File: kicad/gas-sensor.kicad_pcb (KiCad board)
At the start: 2 copper layers, 37 parts, among them J1 Conn FT232RL, J10 hole, J11 hole, J2 RJ12, J3 hole, J4 hole, J5 hole, J6 hole, J7 5V_Power_source, J8 hole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

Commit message: Update after debugging
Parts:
- moved J10 9.09 mm to (59.9, 66.5)
- moved J8 9.09 mm to (140.2, 66.5)
- moved J11 9.09 mm to (59.9, 94.2)
- moved J9 9.09 mm to (140.2, 94.2)
- moved U3 2.13 mm to (72.6, 94.2)
- moved GS1 1.48 mm to (130.8, 84.9)
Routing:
- net Net-(GS1-Pad6): track 31.7 -> 29.8 mm
- net /HUM: track 85.7 -> 86.7 mm
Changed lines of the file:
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@@
-(kicad_pcb (version 20171130) (host pcbnew "(5.0.2-4-g3082e92af)")
+(kicad_pcb (version 20171130) (host pcbnew "(5.0.1-3-g963ef8bb5)")
   (general
     (thickness 1.6)
     (drawings 12)
-    (tracks 384)
+    (tracks 383)
     (zones 0)
     (modules 37)
@@
   )
   (setup
-    (last_trace_width 0.25)
+    (last_trace_width 1)
     (user_trace_width 0.25)
     (user_trace_width 0.5)
@@
     (add_net VCC)
   )
+  (module footprints:DHT22_HOR (layer F.Cu)
+    (at 72.61 94.22)
+    (fp_text reference U3 (at -0.72 1.86) (layer F.SilkS)
+      (effects (font (size 1 1) (thickness 0.15)))
+    )
+    (fp_text value DHT22 (at -0.79 -1.8) (layer F.Fab)
+      (effects (font (size 1 1) (thickness 0.15)))
+    )
+    (fp_line (start 6.3 -30) (end 6.3 3) (layer F.SilkS) (width 0.15))
+    (fp_line (start -8.8 -30) (end -8.8 3) (layer F.SilkS) (width 0.15))
+    (fp_line (start -8.8 -30) (end 6.3 -30) (layer F.SilkS) (width 0.15))
+    (fp_line (start 6.3 3) (end -8.8 3) (layer F.SilkS) (width 0.15))
+    (pad 4 thru_hole rect (at 2.54 0) (size 1.5 1.5) (drill oval 1 0.8) (layers *.Cu *.Mask)
+      (net 1 GND))
+    (pad 3 thru_hole rect (at 0 0) (size 1.5 1.5) (drill oval 1 0.8) (layers *.Cu *.Mask)
+      (net 46 "Net-(U3-Pad3)"))
+    (pad 2 thru_hole rect (at -2.54 0) (size 1.5 1.5) (drill oval 1 0.8) (layers *.Cu *.Mask)
+      (net 25 /HUM))
+    (pad 1 thru_hole rect (at -5 0) (size 1.5 1.5) (drill oval 1 0.8) (layers *.Cu *.Mask)
+      (net 7 +5V))
+    (model ${KIPRJMOD}/shapes3D/DHT22_HOR.wrl
+      (offset (xyz -9 5 0))
+      (scale (xyz 400 400 400))
+      (rotate (xyz 0 0 0))
+    )
+  )
   (module footprints:MH-Z19 (layer F.Cu)
     (at 90.25 80.37 270)
@@
       (at (xyz 0 0 0))
       (scale (xyz 1 1 1))
-      (rotate (xyz 0 0 0))
-    )
-  )
-  (module footprints:DHT22_HOR (layer F.Cu)
-    (at 70.48 94.34)
-    (fp_text reference U3 (at -0.72 1.86) (layer F.SilkS)
-      (effects (font (size 1 1) (thickness 0.15)))
-    )
-    (fp_text value DHT22 (at -0.79 -1.8) (layer F.Fab)
-      (effects (font (size 1 1) (thickness 0.15)))
-    )
-    (fp_line (start 6.3 3) (end -8.8 3) (layer F.SilkS) (width 0.15))
-    (fp_line (start -8.8 -30) (end 6.3 -30) (layer F.SilkS) (width 0.15))
-    (fp_line (start -8.8 -30) (end -8.8 3) (layer F.SilkS) (width 0.15))
-    (fp_line (start 6.3 -30) (end 6.3 3) (layer F.SilkS) (width 0.15))
-    (pad 4 thru_hole rect (at 2.5 0) (size 1 1) (drill 0.5) (layers *.Cu *.Mask)
-      (net 1 GND))
-    (pad 3 thru_hole rect (at 0 0) (size 1 1) (drill 0.5) (layers *.Cu *.Mask)
-      (net 46 "Net-(U3-Pad3)"))
-    (pad 2 thru_hole rect (at -2.5 0) (size 1 1) (drill 0.5) (layers *.Cu *.Mask)
-      (net 25 /HUM))
-    (pad 1 thru_hole rect (at -5 0) (size 1 1) (drill 0.5) (layers *.Cu *.Mask)
-      (net 7 +5V))
-    (model ${KIPRJMOD}/shapes3D/DHT22_HOR.wrl
-      (offset (xyz -9 5 0))
-      (scale (xyz 400 400 400))
       (rotate (xyz 0 0 0))
     )
@@
   )
   (module MountingHole:MountingHole_3.2mm_M3 (layer F.Cu)
-    (at 146.65 60.15)
+    (at 140.15 66.5)
     (descr "Mounting Hole 3.2mm, no annular, M3")
     (tags "mounting hole 3.2mm no annular m3")
@@
   )
   (module MountingHole:MountingHole_3.2mm_M3 (layer F.Cu)
-    (at 146.65 100.5)
+    (at 140.15 94.15)
     (descr "Mounting Hole 3.2mm, no annular, M3")
     (tags "mounting hole 3.2mm no annular m3")
@@
   )
   (module MountingHole:MountingHole_3.2mm_M3 (layer F.Cu)
-    (at 53.35 60.15)
+    (at 59.85 66.5)
     (descr "Mounting Hole 3.2mm, no annular, M3")
     (tags "mounting hole 3.2mm no annular m3")
@@
   )
   (module MountingHole:MountingHole_3.2mm_M3 (layer F.Cu)
-    (at 53.35 100.5)
+    (at 59.85 94.15)
     (descr "Mounting Hole 3.2mm, no annular, M3")
     (tags "mounting hole 3.2mm no annular m3")
@@
   )
   (module footprints:MQ-4 (layer F.Cu)
-    (at 132.28 85.13 180)
+    (at 130.82 84.89 180)
     (fp_text reference GS1 (at 0 1.27 180) (layer F.SilkS)
       (effects (font (size 1 1) (thickness 0.15)))
@@
   )
   (gr_line (start 56.7 63.15) (end 143.7 63.15) (layer F.SilkS) (width 0.2))
-  (gr_line (start 143.7 63.15) (end 143.7 97.5) (layer F.SilkS) (width 0.2))
+  (gr_line (start 143.5 63.15) (end 143.5 97.5) (layer F.SilkS) (width 0.2))
   (gr_line (start 56.7 97.5) (end 143.3 97.5) (layer F.SilkS) (width 0.2))
-  (gr_line (start 56.7 63.15) (end 56.7 97.5) (layer F.SilkS) (width 0.2))
+  (gr_line (start 56.5 63.15) (end 56.5 97.5) (layer F.SilkS) (width 0.2))
   (gr_line (start 150 103.5) (end 50 103.5) (layer F.SilkS) (width 0.2))
   (gr_line (start 50 57.15) (end 150 57.15) (layer F.SilkS) (width 0.2))
@@
   (segment (start 116.55499 118.41501) (end 116.55499 118.34649) (width 1) (layer F.Cu) (net 16))
   (segment (start 115.78 119.19) (end 116.55499 118.41501) (width 1) (layer F.Cu) (net 16))
-  (segment (start 134.638751 87.488751) (end 135.63875 88.48875) (width 1) (layer F.Cu) (net 16))
-  (segment (start 129.921249 87.488751) (end 134.638751 87.488751) (width 1) (layer F.Cu) (net 16))
-  (segment (start 128.92125 88.48875) (end 129.921249 87.488751) (width 1) (layer F.Cu) (net 16))
-  (segment (start 116.55499 100.85501) (end 128.92125 88.48875) (width 1) (layer F.Cu) (net 16))
   (segment (start 116.55499 118.41501) (end 116.55499 100.85501) (width 1) (layer F.Cu) (net 16))
+  (segment (start 127.46125 89.94875) (end 127.46125 88.24875) (width 1) (layer F.Cu) (net 16))
+  (segment (start 116.55499 100.85501) (end 127.46125 89.94875) (width 1) (layer F.Cu) (net 16))
+  (segment (start 133.178751 87.248751) (end 134.17875 88.24875) (width 1) (layer F.Cu) (net 16))
+  (segment (start 128.461249 87.248751) (end 133.178751 87.248751) (width 1) (layer F.Cu) (net 16))
+  (segment (start 127.46125 88.24875) (end 128.461249 87.248751) (width 1) (layer F.Cu) (net 16))
   (segment (start 93.142934 126.012755) (end 92.73 125.599821) (width 0.5) (layer F.Cu) (net 17))
   (segment (start 93.917934 126.012755) (end 93.142934 126.012755) (width 0.5) (layer F.Cu) (net 17))
@@
   (via (at 78.41 137.98) (size 0.8) (drill 0.4) (layers F.Cu B.Cu) (net 25))
   (segment (start 81.5 137.98) (end 78.41 137.98) (width 0.5) (layer B.Cu) (net 25))
-  (segment (start 78.38 138.01) (end 78.41 137.98) (width 0.5) (layer F.Cu) (net 25))
-  (segment (start 73.88 138.01) (end 78.38 138.01) (width 0.5) (layer F.Cu) (net 25))
-  (segment (start 63.57999 127.70999) (end 63.49999 127.70999) (width 0.5) (layer F.Cu) (net 25))
-  (segment (start 73.88 138.01) (end 63.57999 127.70999) (width 0.5) (layer F.Cu) (net 25))
-  (segment (start 63.49999 127.70999) (end 61.33 125.54) (width 0.5) (layer F.Cu) (net 25))
-  (segment (start 61.33 125.54) (end 53.25 125.54) (width 0.5) (layer F.Cu) (net 25))
-  (segment (start 67.98 95.34) (end 67.98 94.34) (width 0.5) (layer F.Cu) (net 25))
-  (segment (start 67.98 100.111002) (end 67.98 95.34) (width 0.5) (layer F.Cu) (net 25))
-  (segment (start 51.869999 116.221003) (end 67.98 100.111002) (width 0.5) (layer F.Cu) (net 25))
+  (segment (start 51.869999 116.221003) (end 70.07 98.021002) (width 0.5) (layer F.Cu) (net 25))
   (segment (start 51.869999 124.159999) (end 51.869999 116.221003) (width 0.5) (layer F.Cu) (net 25))
   (segment (start 53.25 125.54) (end 51.869999 124.159999) (width 0.5) (layer F.Cu) (net 25))
-  (segment (start 128.53 116.57) (end 127.03 116.57) (width 0.5) (layer F.Cu) (net 26))
-  (segment (start 131.890002 116.57) (end 128.53 116.57) (width 0.5) (layer F.Cu) (net 26))
-  (segment (start 132.28 116.180002) (end 131.890002 116.57) (width 0.5) (layer F.Cu) (net 26))
-  (segment (start 132.28 89.88) (end 132.28 116.180002) (width 0.5) (layer F.Cu) (net 26))
+  (segment (start 63.49999 127.70999) (end 61.33 125.54) (width 0.5) (layer F.Cu) (net 25))
+  (segment (start 73.88 138.01) (end 63.57999 127.70999) (width 0.5) (layer F.Cu) (net 25))
+  (segment (start 70.07 98.021002) (end 70.07 94.22) (width 0.5) (layer F.Cu) (net 25))
+  (segment (start 61.33 125.54) (end 53.25 125.54) (width 0.5) (layer F.Cu) (net 25))
+  (segment (start 63.57999 127.70999) (end 63.49999 127.70999) (width 0.5) (layer F.Cu) (net 25))
+  (segment (start 78.38 138.01) (end 73.88 138.01) (width 0.5) (layer F.Cu) (net 25))
+  (segment (start 78.41 137.98) (end 78.38 138.01) (width 0.5) (layer F.Cu) (net 25))
+  (segment (start 129.17 116.57) (end 127.03 116.57) (width 0.5) (layer F.Cu) (net 26))
+  (segment (start 130.82 114.92) (end 129.17 116.57) (width 0.5) (layer F.Cu) (net 26))
+  (segment (start 130.82 89.64) (end 130.82 114.92) (width 0.5) (layer F.Cu) (net 26))
   (segment (start 102.052936 128.262755) (end 102.94 127.375691) (width 0.5) (layer F.Cu) (net 27))
   (segment (start 100.967934 128.262755) (end 102.052936 128.262755) (width 0.5) (layer F.Cu) (net 27))

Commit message: Update
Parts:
- added R6: 4,7k, Resistor_SMD:R_0805_2012Metric_Pad1.15x1.40mm_HandSolder, F.Cu at (105.8, 104.8)
- R2: value R -> 4,7
- R4: value 20k -> 22k
- moved J7 3.11 mm to (64.8, 131.2)
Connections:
- DS1 pad 10: Net-(DS1-Pad10) -> (no net)
- DS1 pad 3: VCC -> (no net)
- DS1 pad 5: /LCD_RW -> GND
- DS1 pad 7: Net-(DS1-Pad7) -> (no net)
- DS1 pad 8: Net-(DS1-Pad8) -> (no net)
- DS1 pad 9: Net-(DS1-Pad9) -> (no net)
- GS3 pad 2: /RX_MH-Z19 -> /TX_MH-Z19
- GS3 pad 3: /TX_MH-Z19 -> /RX_MH-Z19
- GS3 pad 4: Net-(GS3-Pad4) -> (no net)
- GS3 pad 5: Net-(GS3-Pad5) -> (no net)
- GS3 pad 6: VCC -> +5V
- GS3 pad 8: Net-(GS3-Pad8) -> (no net)
- J1 pad 2: Net-(J1-Pad2) -> (no net)
- J10 pad 1: Net-(J10-Pad1) -> (no net)
- J11 pad 1: Net-(J11-Pad1) -> (no net)
- J2 pad 1: Net-(J2-Pad1) -> (no net)
- J2 pad 5: Net-(J2-Pad5) -> (no net)
- J3 pad 1: Net-(J3-Pad1) -> (no net)
- J4 pad 1: Net-(J4-Pad1) -> (no net)
- J5 pad 1: Net-(J5-Pad1) -> (no net)
- J6 pad 1: Net-(J6-Pad1) -> (no net)
- J8 pad 1: Net-(J8-Pad1) -> (no net)
- J9 pad 1: Net-(J9-Pad1) -> (no net)
- U2 pad 11: /LCD_RW -> (no net)
- U2 pad 19: /Sensor1_ON -> /Sensor2
- U2 pad 23: /Sensor2 -> /Sensor1_ON
- U2 pad 25: /TX_MH-Z19 -> /RX_MH-Z19
- U2 pad 26: /RX_MH-Z19 -> /TX_MH-Z19
- U3 pad 3: Net-(U3-Pad3) -> (no net)
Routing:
- net VCC: track 180.6 -> 115.1 mm, vias 8 -> 6
- net +5V: track 0.00 -> 17.8 mm
- net /LCD_RW: track 11.5 -> 0.00 mm
- net /Sensor2: track 65.6 -> 70.2 mm, vias 0 -> 2
- net GND: track 61.3 -> 64.0 mm, vias 8 -> 9
- net /Sensor1_ON: track 30.6 -> 29.3 mm, vias 0 -> 2
- net /TX_MH-Z19: track 36.5 -> 37.3 mm
- net /RX_MH-Z19: track 37.3 -> 36.5 mm

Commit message: Update
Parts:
- added R7: 3362P-103, TRIM_3362R-1-222:TRIM_3362R-1-222, F.Cu at (83.5, 145.6)
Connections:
- DS1 pad 3: (no net) -> Net-(DS1-Pad3)
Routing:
- net Net-(DS1-Pad3): track 0.00 -> 6.73 mm
- net VCC: track 115.1 -> 120.8 mm
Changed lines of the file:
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@@
     (thickness 1.6)
     (drawings 12)
-    (tracks 394)
+    (tracks 398)
     (zones 0)
-    (modules 38)
-    (nets 34)
+    (modules 39)
+    (nets 35)
   )
   (page A4)
@@
   )
   (setup
-    (last_trace_width 0.5)
+    (last_trace_width 1)
     (user_trace_width 0.25)
     (user_trace_width 0.5)
@@
   (net 32 /LCD4_SCK)
   (net 33 /LCD3_MISO)
+  (net 34 "Net-(DS1-Pad3)")
   (net_class Default "Ceci est la Netclass par défaut."
     (clearance 0.2)
@@
     (add_net GND)
     (add_net "Net-(DS1-Pad15)")
+    (add_net "Net-(DS1-Pad3)")
     (add_net "Net-(GS1-Pad6)")
     (add_net "Net-(GS2-Pad6)")
@@
     (pad 4 thru_hole oval (at 7.62 0) (size 1.8 2.6) (drill 1.2) (layers *.Cu *.Mask)
       (net 27 /LCD_RS))
-    (pad 3 thru_hole oval (at 5.08 0) (size 1.8 2.6) (drill 1.2) (layers *.Cu *.Mask))
+    (pad 3 thru_hole oval (at 5.08 0) (size 1.8 2.6) (drill 1.2) (layers *.Cu *.Mask)
+      (net 34 "Net-(DS1-Pad3)"))
     (pad 2 thru_hole oval (at 2.54 0) (size 1.8 2.6) (drill 1.2) (layers *.Cu *.Mask)
       (net 18 VCC))
@@
       (scale (xyz 1 1 1))
       (rotate (xyz 0 0 0))
+    )
+  )
+  (module TRIM_3362R-1-222:TRIM_3362R-1-222 (layer F.Cu)
+    (at 83.5 145.59)
+    (fp_text reference R7 (at -1.4655 -4.65107) (layer F.SilkS)
+      (effects (font (size 0.8 0.8) (thickness 0.05)))
+    )
+    (fp_text value 3362P-103 (at -0.75282 4.62667) (layer F.SilkS)
+      (effects (font (size 0.8 0.8) (thickness 0.05)))
+    )
+    (fp_line (start 3.3 3.495) (end -3.3 3.495) (layer F.SilkS) (width 0.127))
+    (fp_line (start -3.3 3.495) (end -3.3 1.02) (layer F.SilkS) (width 0.127))
+    (fp_line (start -3.3 -1.02) (end -3.3 -3.495) (layer F.SilkS) (width 0.127))
+    (fp_line (start -3.3 -3.495) (end 3.3 -3.495) (layer F.SilkS) (width 0.127))
+    (fp_line (start 3.3 -3.495) (end 3.3 -1.02) (layer F.SilkS) (width 0.127))
+    (fp_line (start 3.3 1.02) (end 3.3 3.495) (layer F.SilkS) (width 0.127))
+    (fp_line (start 3.55 3.745) (end -3.55 3.745) (layer Eco1.User) (width 0.05))
+    (fp_line (start -3.55 3.745) (end -3.55 -3.745) (layer Eco1.User) (width 0.05))
+    (fp_line (start -3.55 -3.745) (end 3.55 -3.745) (layer Eco1.User) (width 0.05))
+    (fp_line (start 3.55 -3.745) (end 3.55 3.745) (layer Eco1.User) (width 0.05))
+    (fp_circle (center -4.064 0) (end -3.964 0) (layer F.SilkS) (width 0.2))
+    (fp_line (start -3.3 -3.495) (end -3.3 3.495) (layer Eco2.User) (width 0.127))
+    (fp_line (start -3.3 3.495) (end 3.3 3.495) (layer Eco2.User) (width 0.127))
+    (fp_line (start 3.3 3.495) (end 3.3 -3.495) (layer Eco2.User) (width 0.127))
+    (fp_line (start 3.3 -3.495) (end -3.3 -3.495) (layer Eco2.User) (width 0.127))
+    (fp_circle (center -4.064 0) (end -3.964 0) (layer Eco2.User) (width 0.2))
+    (pad 3 thru_hole circle (at 2.54 -0.065 180) (size 1.198 1.198) (drill 0.69) (layers *.Cu *.Mask)
+      (net 34 "Net-(DS1-Pad3)"))
+    (pad 2 thru_hole circle (at 0 2.475 180) (size 1.198 1.198) (drill 0.69) (layers *.Cu *.Mask))
+    (pad 1 thru_hole rect (at -2.54 -0.065 180) (size 1.198 1.198) (drill 0.69) (layers *.Cu *.Mask)
+      (net 18 VCC))
+    (model ${KIPRJMOD}/shapes3D/3362P-1-102LF.STEP
+      (at (xyz 0 0 0))
+      (scale (xyz 1 1 1))
+      (rotate (xyz -90 0 180))
     )
   )
@@
   (segment (start 125.04214 143.74786) (end 123.08 145.71) (width 1) (layer F.Cu) (net 18) (status 20))
   (segment (start 128.691839 143.74786) (end 125.04214 143.74786) (width 1) (layer F.Cu) (net 18) (status 10))
+  (segment (start 80.287934 144.852934) (end 80.96 145.525) (width 1) (layer F.Cu) (net 18))
+  (segment (start 80.287934 140.122755) (end 80.287934 144.852934) (width 1) (layer F.Cu) (net 18))
   (via (at 90.92 122.49) (size 0.8) (drill 0.4) (layers F.Cu B.Cu) (net 19))
   (segment (start 92.467934 126.687755) (end 90.92 125.139821) (width 0.5) (layer F.Cu) (net 19))
@@
   (segment (start 117.181786 125.890011) (end 115.510089 125.890011) (width 0.5) (layer F.Cu) (net 33))
   (segment (start 115.510089 125.890011) (end 114.126033 127.274067) (width 0.5) (layer F.Cu) (net 33))
+  (segment (start 82.827934 142.312934) (end 86.04 145.525) (width 1) (layer F.Cu) (net 34))
+  (segment (start 82.827934 140.122755) (end 82.827934 142.312934) (width 1) (layer F.Cu) (net 34))
   (zone (net 7) (net_name +5V) (layer F.Cu) (hatch edge 0.508)
     (connect_pads (clearance 0.508))

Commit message: gerver v1.1.0
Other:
- board text added: "Gas sensor v1.1.0"
- board text removed: "Gas sensor v1.0.0"
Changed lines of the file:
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@@
-(kicad_pcb (version 20171130) (host pcbnew "(5.0.1-3-g963ef8bb5)")
+(kicad_pcb (version 20171130) (host pcbnew 5.0.2-5.fc29)
   (general
     (thickness 1.6)
@@
   )
   (setup
-    (last_trace_width 1)
+    (last_trace_width 0.25)
     (user_trace_width 0.25)
     (user_trace_width 0.5)
@@
     (arrow2b (pts (xy 174.536 150.152) (xy 173.949579 149.025496)))
   )
-  (gr_text "Gas sensor v1.0.0" (at 68.364 147.104) (layer F.SilkS)
+  (gr_text "Gas sensor v1.1.0" (at 68.364 147.104) (layer F.SilkS)
     (effects (font (size 1.5 1.5) (thickness 0.3)))
   )

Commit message: Rx/Tx + Potentiometer ok
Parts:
- removed R7: 3362P-103, TRIM_3362R-1-222:TRIM_3362R-1-222
- added RV1: R_POT, TRIM_3362R-1-222:TRIM_3362R-1-222, F.Cu at (82.9, 146.4)
- R4: value 22k -> 4.7k
- moved J5 0.07 mm to (146.6, 146.6)
- moved J3 0.07 mm to (53.4, 146.6)
- moved J4 0.07 mm to (146.6, 53.4)
- moved J6 0.07 mm to (53.4, 53.4)
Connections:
- J1 pad 4: /TX -> /RX
- J1 pad 5: /RX -> /TX
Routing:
- net Net-(DS1-Pad3): track 6.73 -> 3.80 mm
- net /TX: track 39.7 -> 42.3 mm
- net /RX: track 44.2 -> 41.9 mm, vias 0 -> 1
- net GND: track 64.0 -> 62.1 mm, vias 9 -> 8
- net VCC: track 120.8 -> 121.5 mm
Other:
- board outline added: 100 x 100 mm
- board text added: "Gas sensor v1.0.0"
- board text removed: "Gas sensor v1.1.0"

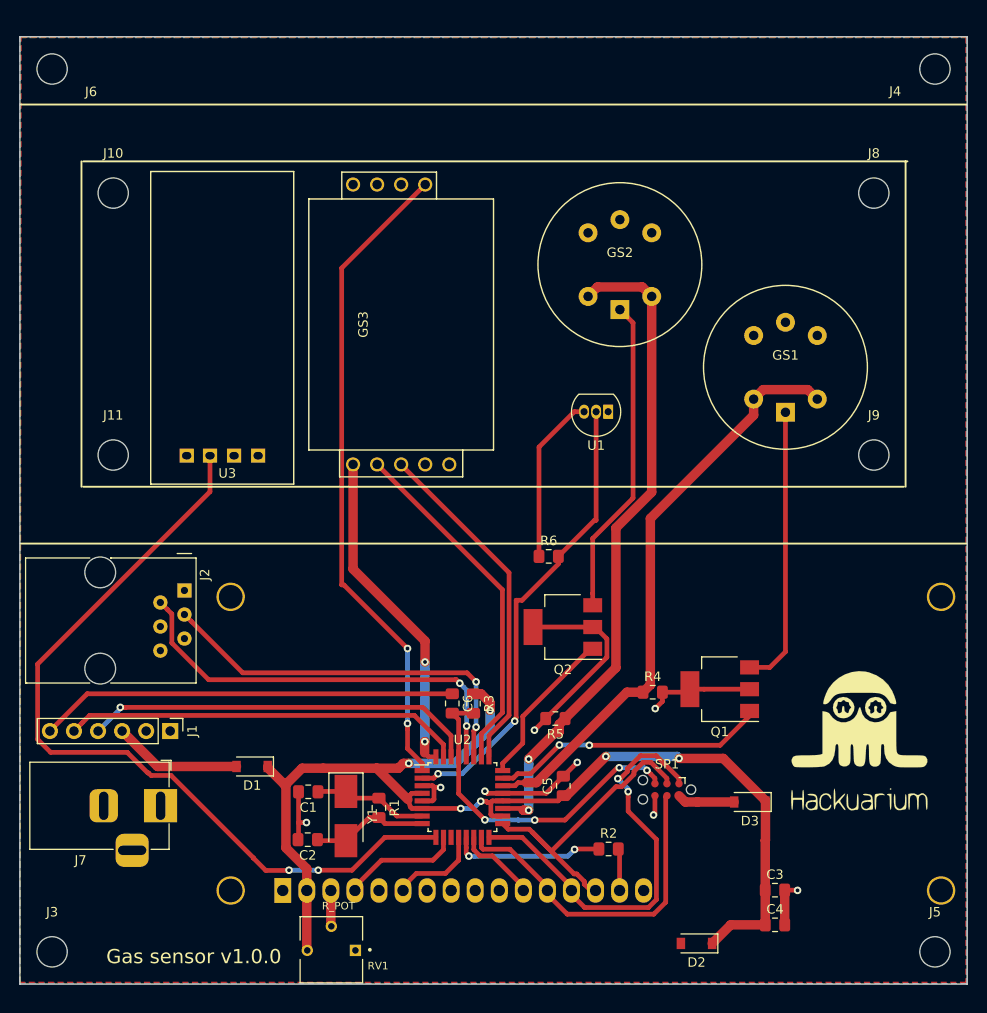
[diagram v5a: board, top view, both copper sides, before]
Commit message: Added voltage regulator
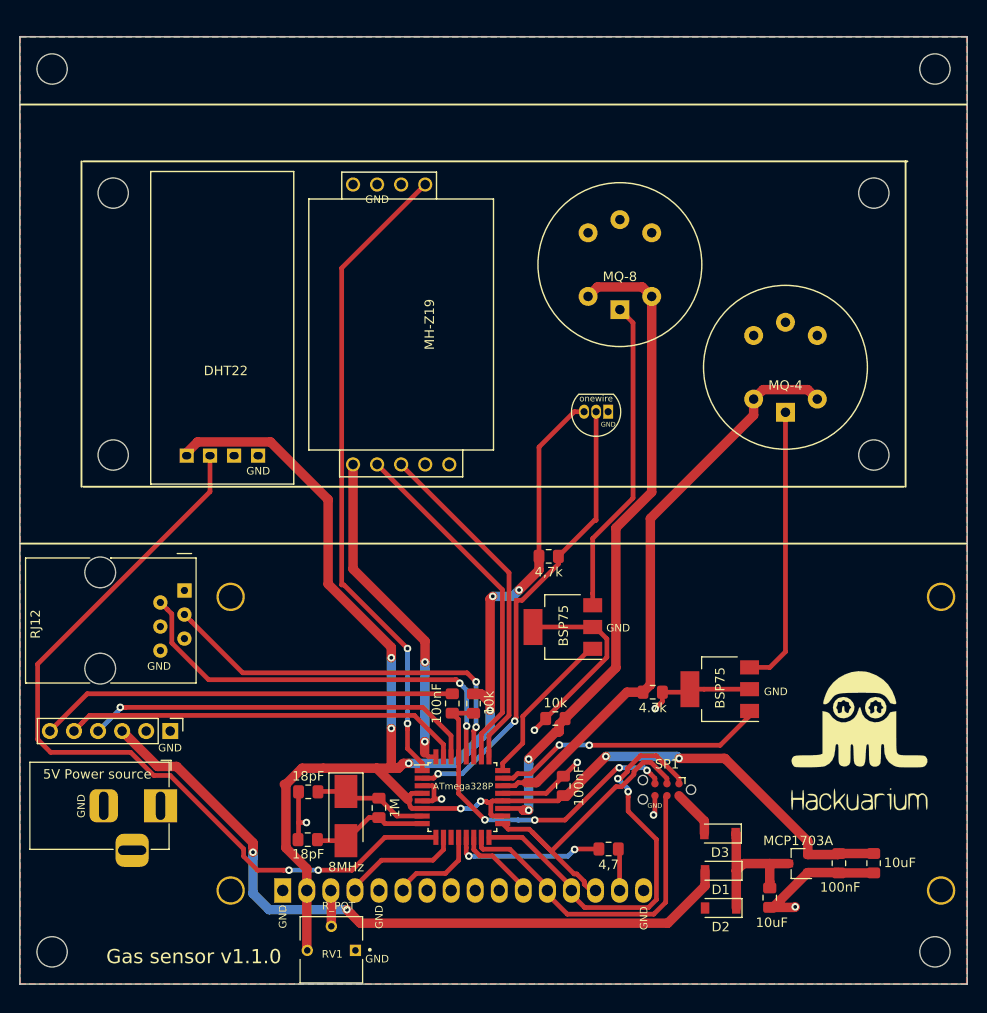
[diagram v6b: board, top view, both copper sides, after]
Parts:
- added C7: 10uF, Capacitor_SMD:C_0805_2012Metric_Pad1.15x1.40mm_HandSolder, F.Cu at (129.2, 140.9)
- added U4: MCP1703A, Package_TO_SOT_SMD:SOT-23, F.Cu at (132.2, 137.3)
- C3: value 10u -> 10uF
- J7: value 5V_Power_source -> 5V Power source
- U2: value ATmega328P-AU -> ATmega328P
- moved D1 50.7 mm to (124.0, 138.0)
- moved C3 10.8 mm to (140.1, 137.2), turned to 270 degrees
- moved C4 9.37 mm to (136.5, 137.2), turned to 270 degrees
- moved D3 4.58 mm to (123.9, 134.1)
- moved D2 4.53 mm to (124.0, 142.0)
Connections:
- D1 pad 1: VCC -> Net-(C7-Pad1)
- D2 pad 1: VCC -> Net-(C7-Pad1)
- D3 pad 1: VCC -> Net-(C7-Pad1)
- R6 pad 1: +5V -> VCC
- U1 pad 3: +5V -> VCC
- U3 pad 1: +5V -> VCC
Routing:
- net VCC: track 121.5 -> 200.0 mm, vias 6 -> 10
- net /VCC-FTDI: track 13.6 -> 76.3 mm, vias 0 -> 2
- net +5V: track 17.8 -> 0.00 mm
- net Net-(C7-Pad1): track 0.00 -> 16.3 mm
- net GND: track 62.1 -> 70.5 mm, vias 8 -> 7
- net /VCC-ICSP: track 6.10 -> 5.11 mm
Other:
- board text added: "GND"
- board text added: "Gas sensor v1.1.0"
- board text added: "onewire"
- board text removed: "Gas sensor v1.0.0"

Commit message: Update CAD
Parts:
- removed J10, J11, J8, J9: hole, MountingHole:MountingHole_3.2mm_M3
- C7: value 10uF -> 10u
- J7: value 5V Power source -> 5V_Power_source
- Q1, Q2: footprint Package_TO_SOT_SMD:SOT-223-3_TabPin2 -> Package_TO_SOT_SMD:SOT-223-3_TabPin3
- U2: value ATmega328P -> ATmega328P-AU
- U4: value MCP1703A -> MCP1703A-1202_SOT23
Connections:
- Q1 pad 2: GND -> Net-(GS1-Pad6)
- Q1 pad 3: Net-(GS1-Pad6) -> GND
- Q2 pad 2: GND -> Net-(GS2-Pad6)
- Q2 pad 3: Net-(GS2-Pad6) -> GND
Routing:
- net GND: track 70.5 -> 66.1 mm, vias 7 -> 8
- net Net-(GS2-Pad6): track 33.6 -> 36.0 mm
- net Net-(GS1-Pad6): track 29.8 -> 31.7 mm
